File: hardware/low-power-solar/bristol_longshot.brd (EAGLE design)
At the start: 40 x 82 mm, 143 parts, among them Q1 NX2301P, Q2 NX2301P, Q3 BSS84, Q4 BSS84, Q5 PBSS4130, Q6 PD84001, U1 SAM_D20E, U10 SIT1552, U11 SIT1552, U12 LTC4070EMS8EPBF, U13 ADP1614ACPZ-1.3-R7, U14 TPS71533DCKR, U15 TPS71533DCKR, U16 74LVC1G04GW, U17 74LVC1G04GW, U18 74LVC1G04GW, U19 AS213-92, U2 SI4461, U20 SKY13373, U3 SE880, U4 SST25WF040BT-40I/NP, U5 TG-5006CJ, U6 TPS73118DBVT, U7 ADM6823WYRJZ, U8 SN74LVC1G32DCKR, U9 TPS62243

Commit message: [low-power-solar] finish of partslist
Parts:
- C4, C48: value TBD -> DNP
- L12: value TBD -> 0Ω
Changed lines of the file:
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@@
 <element name="LED2" library="led" package="CHIPLED_0603" value="GREEN" x="12.75" y="65.5" rot="R180"/>
 <element name="R28" library="microbuilder_v3" package="_0402" value="330Ω" x="12.75" y="67.875" rot="R90"/>
-<element name="L12" library="microbuilder_v3" package="_0402@2" value="TBD" x="20" y="7.5"/>
-<element name="C4" library="microbuilder_v3" package="_0402" value="TBD" x="18" y="7.5" rot="R180"/>
-<element name="C48" library="microbuilder_v3" package="_0402" value="TBD" x="22" y="7.5"/>
+<element name="L12" library="microbuilder_v3" package="_0402@2" value="0Ω" x="20" y="7.5"/>
+<element name="C4" library="microbuilder_v3" package="_0402" value="DNP" x="18" y="7.5" rot="R180"/>
+<element name="C48" library="microbuilder_v3" package="_0402" value="DNP" x="22" y="7.5"/>
 <element name="R30" library="microbuilder_v3" package="_0402" value="10kΩ" x="28.75" y="69.75"/>
 <element name="DZ1" library="microbuilder_v3" package="SOD-323" value="5V6, 500mW" x="26" y="70.875"/>

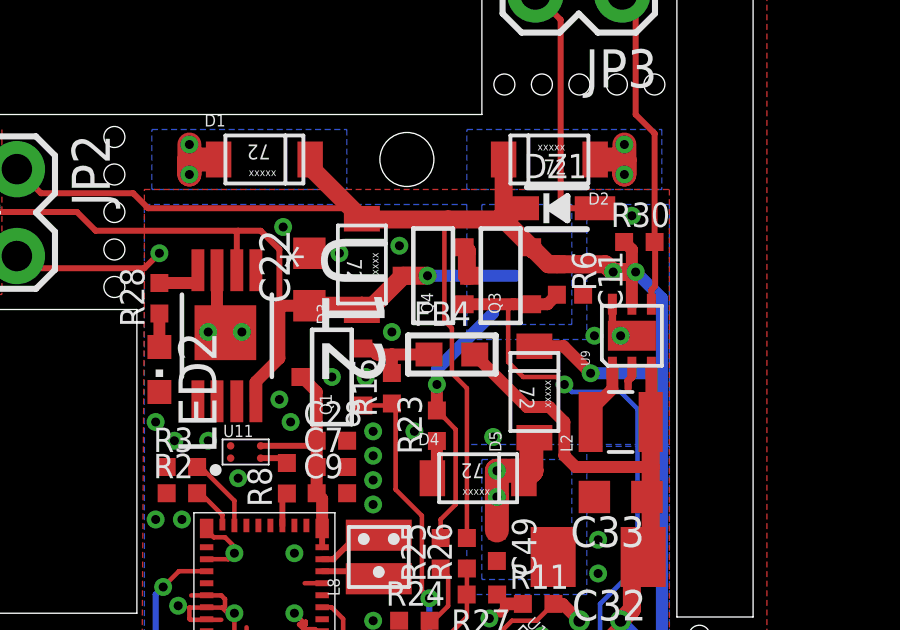
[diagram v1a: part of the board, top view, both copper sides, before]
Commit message: [low-power-solar] update to partslist on ordering
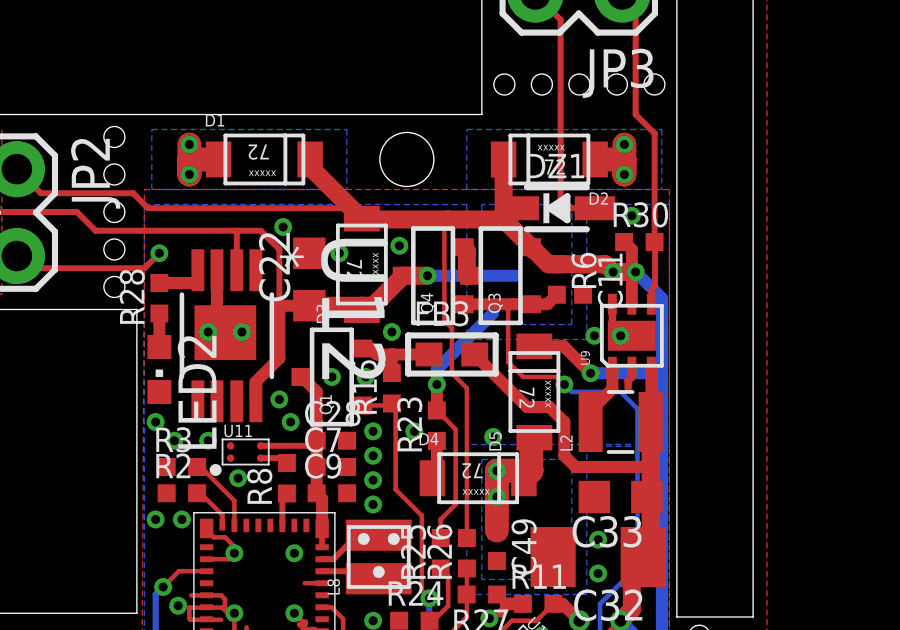
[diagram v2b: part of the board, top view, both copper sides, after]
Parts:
- R20, R21: value (none) -> 22Ω
- renumbered FB4 to FB3
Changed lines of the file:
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@@
 <?xml version="1.0" encoding="utf-8"?>
 <!DOCTYPE eagle SYSTEM "eagle.dtd">
-<eagle version="7.3.0">
+<eagle version="6.5.0">
 <drawing>
 <settings>
@@
 <layer number="23" name="tOrigins" color="15" fill="1" visible="yes" active="yes"/>
 <layer number="24" name="bOrigins" color="15" fill="1" visible="yes" active="yes"/>
-<layer number="25" name="tNames" color="7" fill="1" visible="no" active="yes"/>
-<layer number="26" name="bNames" color="7" fill="1" visible="no" active="yes"/>
-<layer number="27" name="tValues" color="7" fill="1" visible="no" active="yes"/>
-<layer number="28" name="bValues" color="7" fill="1" visible="no" active="yes"/>
+<layer number="25" name="tNames" color="7" fill="1" visible="yes" active="yes"/>
+<layer number="26" name="bNames" color="7" fill="1" visible="yes" active="yes"/>
+<layer number="27" name="tValues" color="7" fill="1" visible="yes" active="yes"/>
+<layer number="28" name="bValues" color="7" fill="1" visible="yes" active="yes"/>
 <layer number="29" name="tStop" color="7" fill="3" visible="yes" active="yes"/>
 <layer number="30" name="bStop" color="7" fill="6" visible="yes" active="yes"/>
@@
 <pass name="Default">
 <param name="RoutingGrid" value="50mil"/>
-<param name="AutoGrid" value="1"/>
-<param name="Efforts" value="0"/>
-<param name="TopRouterVariant" value="1"/>
 <param name="tpViaShape" value="round"/>
 <param name="PrefDir.1" value="|"/>
@@
 <attribute name="SUPPLIER" value="NXP" x="13.625" y="32.625" size="1.016" layer="27" font="vector" ratio="12" rot="R90" display="off"/>
 </element>
-<element name="R20" library="microbuilder_v3" package="_0603MP" value="" x="18.125" y="25.625" rot="R90"/>
-<element name="R21" library="microbuilder_v3" package="_0603MP" value="" x="17.125" y="25.625" rot="R90"/>
+<element name="R20" library="microbuilder_v3" package="_0603MP" value="22Ω" x="18.125" y="25.625" rot="R90"/>
+<element name="R21" library="microbuilder_v3" package="_0603MP" value="22Ω" x="17.125" y="25.625" rot="R90"/>
 <element name="C49" library="microbuilder_v3" package="_0402" value="100nF" x="24" y="59.625" rot="R270"/>
 <element name="D4" library="RB161M" package="RB161M" value="RB161M" x="23.375" y="61.875" rot="R270"/>
@@
 <element name="JP1" library="SparkFun" package="1X02_LOCK" value="BATTERY_TERMINAL" x="4" y="72" rot="R270"/>
 <element name="JP2" library="SparkFun" package="1X02_LOCK" value="SOLAR_TERMINAL" x="8" y="72" rot="R270"/>
-<element name="FB4" library="microbuilder_v3" package="_0603" value="" x="22.5" y="66"/>
+<element name="FB3" library="microbuilder_v3" package="_0603" value="" x="22.5" y="66"/>
 <element name="R31" library="microbuilder_v3" package="_0402" value="1kΩ" x="13.25" y="39.375" rot="R180"/>
 <element name="R32" library="microbuilder_v3" package="_0402" value="1kΩ" x="13.25" y="34.875" rot="R180"/>
@@
 <wire x1="22.117" y1="38.375" x2="22.117" y2="38.427940625" width="0.4" layer="1"/>
 <wire x1="22.117" y1="38.427940625" x2="21.379" y2="36.939940625" width="0.4" layer="1" curve="-30"/>
+<wire x1="21.379" y1="36.939940625" x2="21.378996875" y2="36.939940625" width="0" layer="19" extent="1-1"/>
 </signal>
 <signal name="FILTER2">
@@
 <wire x1="19.5" y1="66.2" x2="19.8" y2="66.2" width="0.4" layer="1"/>
 <wire x1="19.8" y1="66.2" x2="20" y2="66" width="0.4" layer="1"/>
-<contactref element="FB4" pad="1"/>
+<contactref element="FB3" pad="1"/>
 <wire x1="21.738" y1="66" x2="20.5" y2="66" width="0.4" layer="1"/>
 <wire x1="20.5" y1="66" x2="20" y2="66" width="0.4" layer="1"/>
@@
 <wire x1="12.75" y1="46.125" x2="12.5" y2="46.125" width="0.4" layer="16"/>
 <wire x1="12.75" y1="45.258" x2="12.75" y2="46.125" width="0.4" layer="1"/>
-<contactref element="FB4" pad="2"/>
+<contactref element="FB3" pad="2"/>
 <wire x1="25" y1="64.25" x2="23.387" y2="65.863" width="0.4" layer="1"/>
 <wire x1="29.0625" y1="62.1875" x2="29.125" y2="62.25" width="0.4" layer="1"/>

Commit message: [low-power-solar] add values for rx section
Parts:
- C5: value DNP -> 5.1pF
- C6: value DNP -> 2.7pF
- L6, L7: value DNP -> 56nH
- R29, R33: value 100kΩ -> 10kΩ
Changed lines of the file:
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@@
 <?xml version="1.0" encoding="utf-8"?>
 <!DOCTYPE eagle SYSTEM "eagle.dtd">
-<eagle version="6.5.0">
+<eagle version="7.3.0">
 <drawing>
 <settings>
@@
 <setting verticaltext="up"/>
 </settings>
-<grid distance="0.5" unitdist="mm" unit="mm" style="lines" multiple="1" display="yes" altdistance="0.025" altunitdist="inch" altunit="inch"/>
+<grid distance="0.125" unitdist="mm" unit="mm" style="lines" multiple="1" display="yes" altdistance="0.025" altunitdist="inch" altunit="inch"/>
 <layers>
 <layer number="1" name="Top" color="4" fill="1" visible="yes" active="yes"/>
@@
 <layer number="23" name="tOrigins" color="15" fill="1" visible="yes" active="yes"/>
 <layer number="24" name="bOrigins" color="15" fill="1" visible="yes" active="yes"/>
-<layer number="25" name="tNames" color="7" fill="1" visible="yes" active="yes"/>
-<layer number="26" name="bNames" color="7" fill="1" visible="yes" active="yes"/>
-<layer number="27" name="tValues" color="7" fill="1" visible="yes" active="yes"/>
-<layer number="28" name="bValues" color="7" fill="1" visible="yes" active="yes"/>
+<layer number="25" name="tNames" color="7" fill="1" visible="no" active="yes"/>
+<layer number="26" name="bNames" color="7" fill="1" visible="no" active="yes"/>
+<layer number="27" name="tValues" color="7" fill="1" visible="no" active="yes"/>
+<layer number="28" name="bValues" color="7" fill="1" visible="no" active="yes"/>
 <layer number="29" name="tStop" color="7" fill="3" visible="yes" active="yes"/>
-<layer number="30" name="bStop" color="7" fill="6" visible="yes" active="yes"/>
+<layer number="30" name="bStop" color="7" fill="6" visible="no" active="yes"/>
 <layer number="31" name="tCream" color="7" fill="4" visible="yes" active="yes"/>
 <layer number="32" name="bCream" color="7" fill="5" visible="yes" active="yes"/>
@@
 <layer number="42" name="bRestrict" color="1" fill="10" visible="yes" active="yes"/>
 <layer number="43" name="vRestrict" color="2" fill="10" visible="yes" active="yes"/>
-<layer number="44" name="Drills" color="7" fill="1" visible="yes" active="yes"/>
+<layer number="44" name="Drills" color="7" fill="1" visible="no" active="yes"/>
 <layer number="45" name="Holes" color="7" fill="1" visible="yes" active="yes"/>
 <layer number="46" name="Milling" color="3" fill="1" visible="yes" active="yes"/>
@@
 <pass name="Default">
 <param name="RoutingGrid" value="50mil"/>
+<param name="AutoGrid" value="1"/>
+<param name="Efforts" value="0"/>
+<param name="TopRouterVariant" value="1"/>
 <param name="tpViaShape" value="round"/>
 <param name="PrefDir.1" value="|"/>
@@
 <element name="C8" library="microbuilder_v3" package="_0402" value="100pF" x="25.375" y="42.5"/>
 <element name="C9" library="microbuilder_v3" package="_0402" value="100pF" x="18.5" y="61.375"/>
-<element name="L6" library="microbuilder_v3" package="_0402@2" value="DNP" x="20.75" y="42.375"/>
-<element name="C5" library="microbuilder_v3" package="_0402" value="DNP" x="18.875" y="41.5" rot="R180"/>
-<element name="L7" library="microbuilder_v3" package="_0402@2" value="DNP" x="20.25" y="41" rot="R90"/>
-<element name="C6" library="microbuilder_v3" package="_0402" value="DNP" x="21.1875" y="41" rot="R90"/>
+<element name="L6" library="microbuilder_v3" package="_0402@2" value="56nH" x="20.75" y="42.375"/>
+<element name="C5" library="microbuilder_v3" package="_0402" value="5.1pF" x="18.875" y="41.5" rot="R180"/>
+<element name="L7" library="microbuilder_v3" package="_0402@2" value="56nH" x="20.25" y="41" rot="R90"/>
+<element name="C6" library="microbuilder_v3" package="_0402" value="2.7pF" x="21.1875" y="41" rot="R90"/>
 <element name="C28" library="microbuilder_v3" package="_0402" value="2.2µF" x="18.5" y="63.125"/>
 <element name="C21" library="microbuilder_v3" package="_0402" value="100nF" x="14.375" y="48.625" rot="R270"/>
@@
 <element name="Q2" library="nxp" package="SOT23" value="NX2301P" x="28.25" y="43" rot="R90"/>
 <element name="R10" library="microbuilder_v3" package="_0402" value="100kΩ" x="28.75" y="45.125" rot="R180"/>
-<element name="R29" library="microbuilder_v3" package="_0402" value="100kΩ" x="24.875" y="46.375"/>
+<element name="R29" library="microbuilder_v3" package="_0402" value="10kΩ" x="24.875" y="46.375"/>
 <element name="Q5" library="PBSS4130" package="SOT1118" value="PBSS4130" x="24.875" y="48"/>
-<element name="R33" library="microbuilder_v3" package="_0402" value="100kΩ" x="24.875" y="49.625"/>
+<element name="R33" library="microbuilder_v3" package="_0402" value="10kΩ" x="24.875" y="49.625"/>
 </elements>
 <signals>
@@
 <wire x1="22.117" y1="38.375" x2="22.117" y2="38.427940625" width="0.4" layer="1"/>
 <wire x1="22.117" y1="38.427940625" x2="21.379" y2="36.939940625" width="0.4" layer="1" curve="-30"/>
-<wire x1="21.379" y1="36.939940625" x2="21.378996875" y2="36.939940625" width="0" layer="19" extent="1-1"/>
 </signal>
 <signal name="FILTER2">
